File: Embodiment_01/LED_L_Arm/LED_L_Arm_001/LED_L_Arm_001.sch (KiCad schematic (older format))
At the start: 14 parts, among them J1 Conn_01x01_Female, J2 Conn_01x01_Female

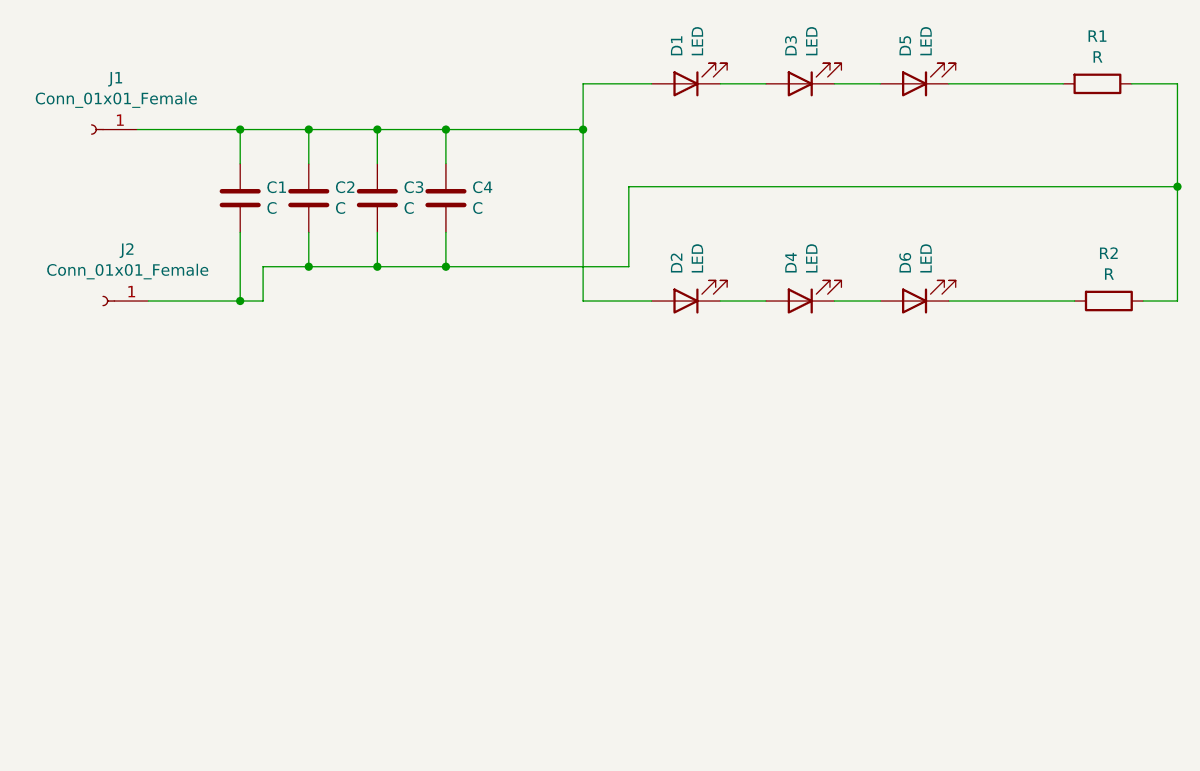
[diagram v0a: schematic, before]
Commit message: Calculation of shape, PCB
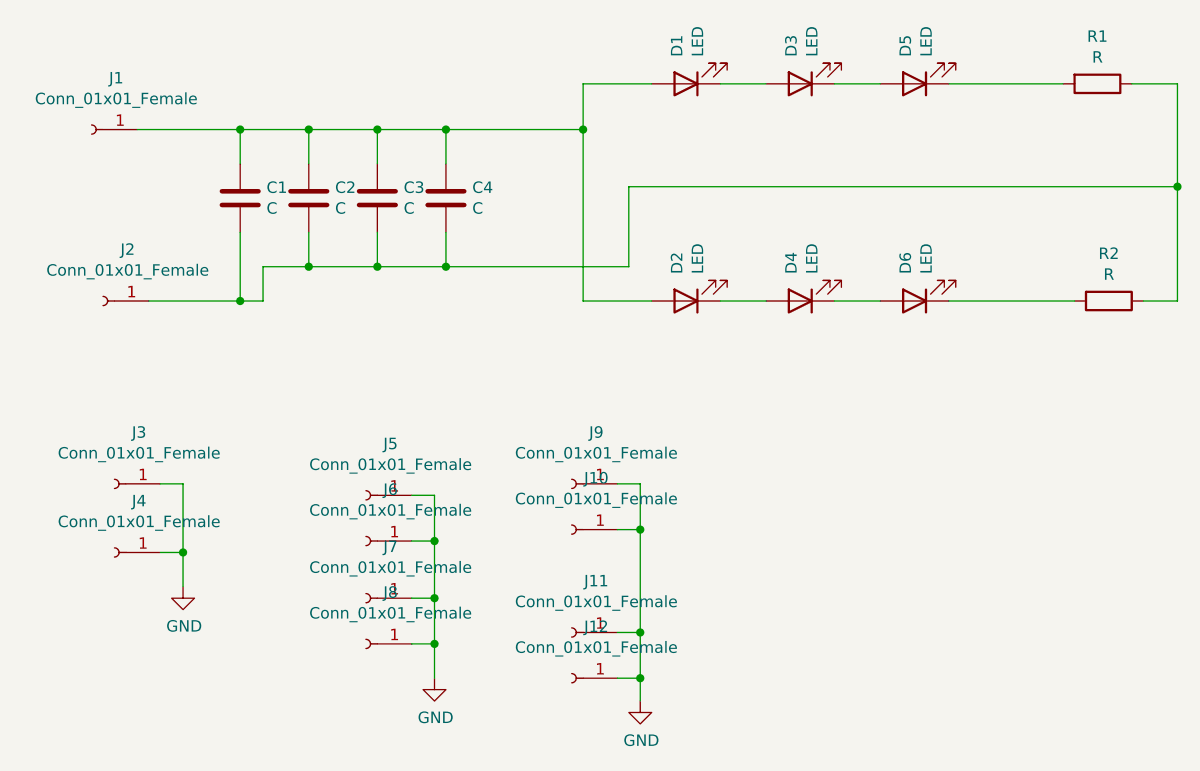
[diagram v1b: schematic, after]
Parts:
- added J10, J11, J12, J9: Conn_01x01_Female, pins:pin_1.0, symbol Connector:Conn_01x01_Female
- added J3, J4, J5, J6: Conn_01x01_Female, pins:WireSidePlate_001, symbol Connector:Conn_01x01_Female
- added J7, J8: Conn_01x01_Female, pins:pin_1.5, symbol Connector:Conn_01x01_Female
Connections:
- new net GND: J10.1 (Pin_1), J11.1 (Pin_1), J12.1 (Pin_1), J3.1 (Pin_1), J4.1 (Pin_1), J5.1 (Pin_1), J6.1 (Pin_1), J7.1 (Pin_1), J8.1 (Pin_1), J9.1 (Pin_1)
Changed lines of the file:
@@
 Wire Wire Line
 	2900 2400 2500 2400
+$Comp
+L Connector:Conn_01x01_Female J3
+U 1 1 6121E8A1
+P 2350 3200
+F 0 "J3" H 2242 2975 50  0000 C CNN
+F 1 "Conn_01x01_Female" H 2242 3066 50  0000 C CNN
+F 2 "pins:WireSidePlate_001" H 2350 3200 50  0001 C CNN
+F 3 "~" H 2350 3200 50  0001 C CNN
+	1    2350 3200
+	-1   0    0    1
+$EndComp
+$Comp
+L Connector:Conn_01x01_Female J4
+U 1 1 6121F038
+P 2350 3500
+F 0 "J4" H 2242 3275 50  0000 C CNN
+F 1 "Conn_01x01_Female" H 2242 3366 50  0000 C CNN
+F 2 "pins:WireSidePlate_001" H 2350 3500 50  0001 C CNN
+F 3 "~" H 2350 3500 50  0001 C CNN
+	1    2350 3500
+	-1   0    0    1
+$EndComp
+$Comp
+L Connector:Conn_01x01_Female J5
+U 1 1 6121F999
+P 3450 3250
+F 0 "J5" H 3342 3025 50  0000 C CNN
+F 1 "Conn_01x01_Female" H 3342 3116 50  0000 C CNN
+F 2 "pins:WireSidePlate_001" H 3450 3250 50  0001 C CNN
+F 3 "~" H 3450 3250 50  0001 C CNN
+	1    3450 3250
+	-1   0    0    1
+$EndComp
+$Comp
+L Connector:Conn_01x01_Female J6
+U 1 1 6122010A
+P 3450 3450
+F 0 "J6" H 3342 3225 50  0000 C CNN
+F 1 "Conn_01x01_Female" H 3342 3316 50  0000 C CNN
+F 2 "pins:WireSidePlate_001" H 3450 3450 50  0001 C CNN
+F 3 "~" H 3450 3450 50  0001 C CNN
+	1    3450 3450
+	-1   0    0    1
+$EndComp
+$Comp
+L Connector:Conn_01x01_Female J7
+U 1 1 61220A38
+P 3450 3700
+F 0 "J7" H 3342 3475 50  0000 C CNN
+F 1 "Conn_01x01_Female" H 3342 3566 50  0000 C CNN
+F 2 "pins:pin_1.5" H 3450 3700 50  0001 C CNN
+F 3 "~" H 3450 3700 50  0001 C CNN
+	1    3450 3700
+	-1   0    0    1
+$EndComp
+$Comp
+L Connector:Conn_01x01_Female J8
+U 1 1 6122126C
+P 3450 3900
+F 0 "J8" H 3342 3675 50  0000 C CNN
+F 1 "Conn_01x01_Female" H 3342 3766 50  0000 C CNN
+F 2 "pins:pin_1.5" H 3450 3900 50  0001 C CNN
+F 3 "~" H 3450 3900 50  0001 C CNN
+	1    3450 3900
+	-1   0    0    1
+$EndComp
+$Comp
+L Connector:Conn_01x01_Female J9
+U 1 1 61225C0A
+P 4350 3200
+F 0 "J9" H 4242 2975 50  0000 C CNN
+F 1 "Conn_01x01_Female" H 4242 3066 50  0000 C CNN
+F 2 "pins:pin_1.0" H 4350 3200 50  0001 C CNN
+F 3 "~" H 4350 3200 50  0001 C CNN
+	1    4350 3200
+	-1   0    0    1
+$EndComp
+$Comp
+L Connector:Conn_01x01_Female J10
+U 1 1 61225C10
+P 4350 3400
+F 0 "J10" H 4242 3175 50  0000 C CNN
+F 1 "Conn_01x01_Female" H 4242 3266 50  0000 C CNN
+F 2 "pins:pin_1.0" H 4350 3400 50  0001 C CNN
+F 3 "~" H 4350 3400 50  0001 C CNN
+	1    4350 3400
+	-1   0    0    1
+$EndComp
+$Comp
+L Connector:Conn_01x01_Female J11
+U 1 1 61225C16
+P 4350 3850
+F 0 "J11" H 4242 3625 50  0000 C CNN
+F 1 "Conn_01x01_Female" H 4242 3716 50  0000 C CNN
+F 2 "pins:pin_1.0" H 4350 3850 50  0001 C CNN
+F 3 "~" H 4350 3850 50  0001 C CNN
+	1    4350 3850
+	-1   0    0    1
+$EndComp
+$Comp
+L Connector:Conn_01x01_Female J12
+U 1 1 61225C1C
+P 4350 4050
+F 0 "J12" H 4242 3825 50  0000 C CNN
+F 1 "Conn_01x01_Female" H 4242 3916 50  0000 C CNN
+F 2 "pins:pin_1.0" H 4350 4050 50  0001 C CNN
+F 3 "~" H 4350 4050 50  0001 C CNN
+	1    4350 4050
+	-1   0    0    1
+$EndComp
+$Comp
+L power:GND #PWR0101
+U 1 1 61229AE3
+P 2650 3650
+F 0 "#PWR0101" H 2650 3400 50  0001 C CNN
+F 1 "GND" H 2655 3477 50  0000 C CNN
+F 2 "" H 2650 3650 50  0001 C CNN
+F 3 "" H 2650 3650 50  0001 C CNN
+	1    2650 3650
+	1    0    0    -1
+$EndComp
+$Comp
+L power:GND #PWR0102
+U 1 1 6122A48C
+P 3750 4050
+F 0 "#PWR0102" H 3750 3800 50  0001 C CNN
+F 1 "GND" H 3755 3877 50  0000 C CNN
+F 2 "" H 3750 4050 50  0001 C CNN
+F 3 "" H 3750 4050 50  0001 C CNN
+	1    3750 4050
+	1    0    0    -1
+$EndComp
+$Comp
+L power:GND #PWR0103
+U 1 1 6122A906
+P 4650 4150
+F 0 "#PWR0103" H 4650 3900 50  0001 C CNN
+F 1 "GND" H 4655 3977 50  0000 C CNN
+F 2 "" H 4650 4150 50  0001 C CNN
+F 3 "" H 4650 4150 50  0001 C CNN
+	1    4650 4150
+	1    0    0    -1
+$EndComp
+Wire Wire Line
+	2550 3200 2650 3200
+Wire Wire Line
+	2650 3200 2650 3500
+Wire Wire Line
+	2550 3500 2650 3500
+Connection ~ 2650 3500
+Wire Wire Line
+	2650 3500 2650 3650
+Wire Wire Line
+	3650 3250 3750 3250
+Wire Wire Line
+	3750 3250 3750 3450
+Wire Wire Line
+	3650 3450 3750 3450
+Connection ~ 3750 3450
+Wire Wire Line
+	3750 3450 3750 3700
+Wire Wire Line
+	3650 3700 3750 3700
+Connection ~ 3750 3700
+Wire Wire Line
+	3750 3700 3750 3900
+Wire Wire Line
+	3650 3900 3750 3900
+Connection ~ 3750 3900
+Wire Wire Line
+	3750 3900 3750 4050
+Wire Wire Line
+	4550 3200 4650 3200
+Wire Wire Line
+	4650 3200 4650 3400
+Wire Wire Line
+	4550 4050 4650 4050
+Connection ~ 4650 4050
+Wire Wire Line
+	4650 4050 4650 4150
+Wire Wire Line
+	4550 3850 4650 3850
+Connection ~ 4650 3850
+Wire Wire Line
+	4650 3850 4650 4050
+Wire Wire Line
+	4550 3400 4650 3400
+Connection ~ 4650 3400
+Wire Wire Line
+	4650 3400 4650 3850
 $EndSCHEMATC
